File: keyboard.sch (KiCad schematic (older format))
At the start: 29 parts, among them CN2 KEYBOARD_HEADER, U13 MOS_6529, U20 74HCT273

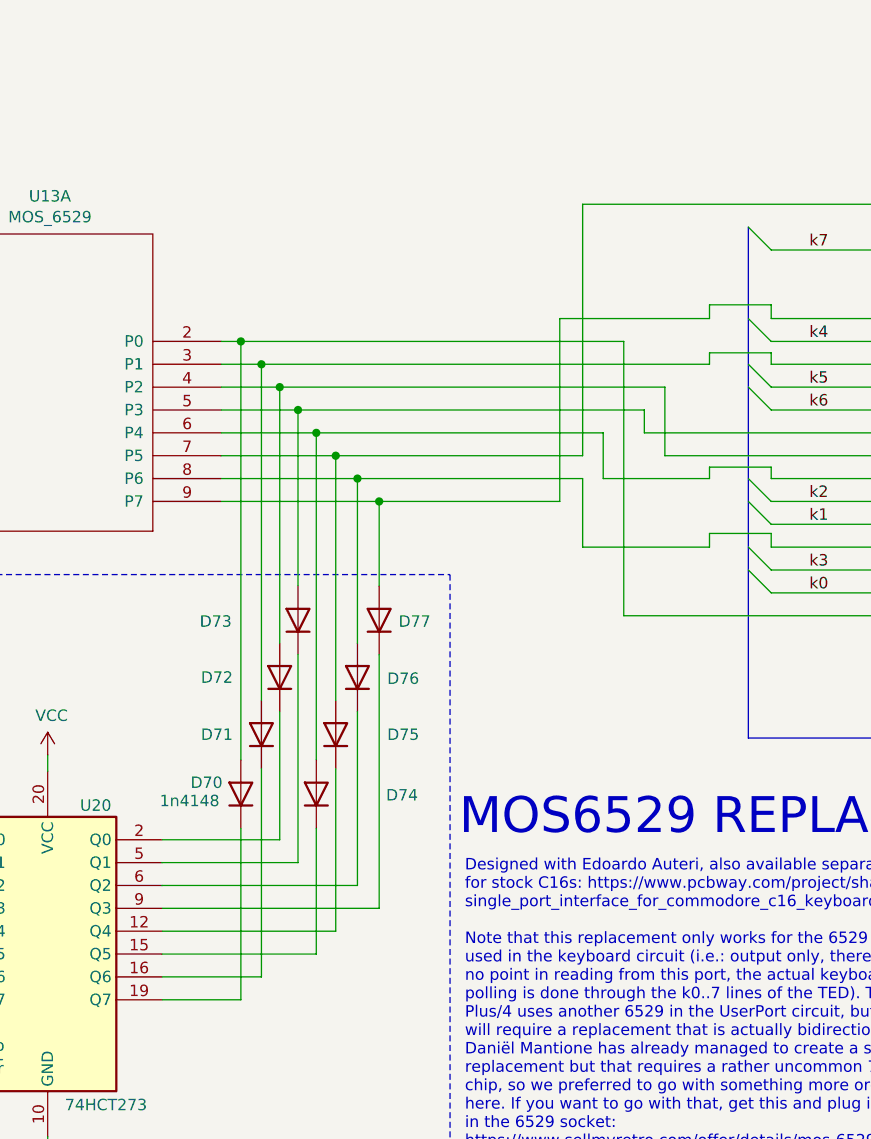
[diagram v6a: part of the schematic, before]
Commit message: Add pull-up network for keyboard buffer Not strictly necessary, boards seems to work fine without, but in principle it should be there
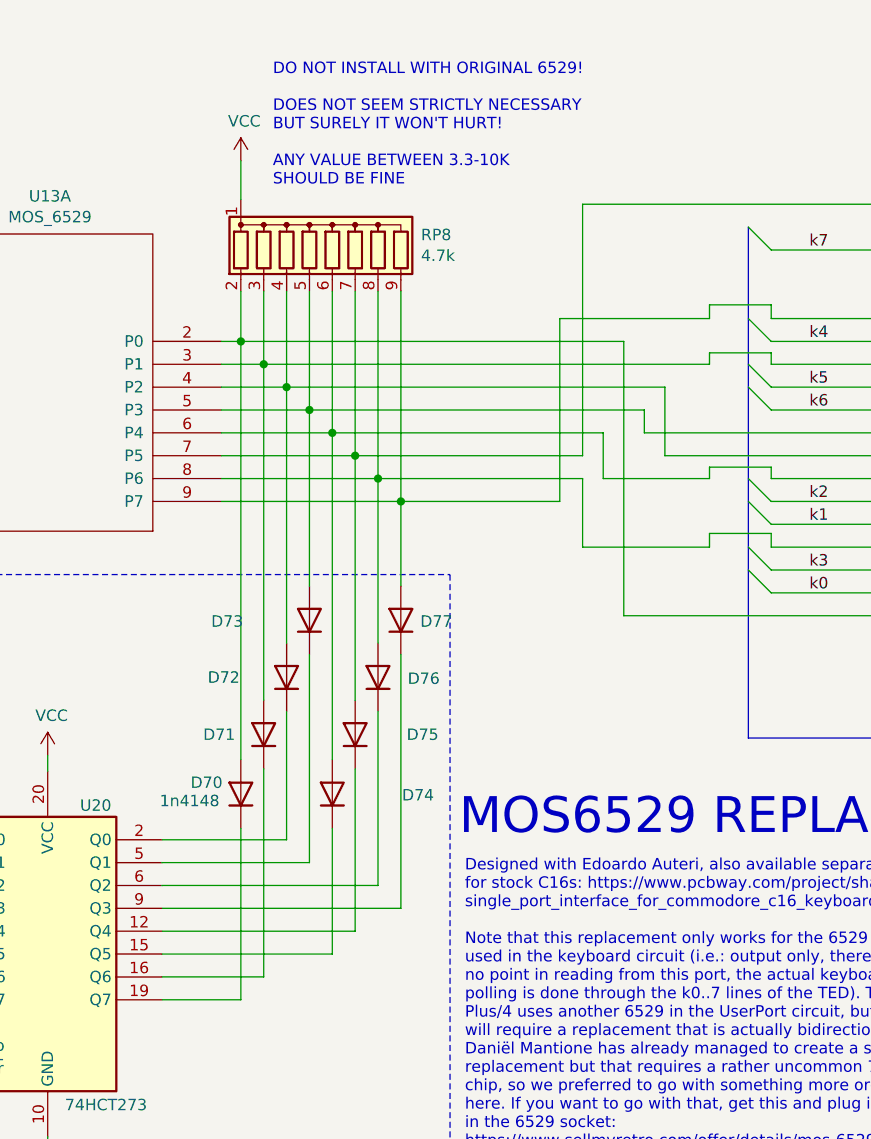
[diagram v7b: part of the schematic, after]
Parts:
- added RP8: 4.7k, Resistor_THT:R_Array_SIP9, symbol Device:R_Network08
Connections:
- net VCC: now also RP8.1 (common)
- net at D70.2 (A), FB41.1, U13.2 (P0): now also RP8.2 (R1)
- net at D71.2 (A), FB42.1, U13.3 (P1): now also RP8.3 (R2)
- net at D72.2 (A), FB43.1, U13.4 (P2): now also RP8.4 (R3)
- net at D73.2 (A), FB44.1, U13.5 (P3): now also RP8.5 (R4)
- net at D74.2 (A), FB45.1, U13.6 (P4): now also RP8.6 (R5)
- net at D75.2 (A), FB46.1, U13.7 (P5): now also RP8.7 (R6)
- net at D76.2 (A), FB47.1, U13.8 (P6): now also RP8.8 (R7)
- net at D77.2 (A), FB48.1, U13.9 (P7): now also RP8.9 (R8)
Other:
- note added: "DO NOT INSTALL WITH ORIGINAL 6529!\n\nDOES NOT SEEM STRICTLY NECESSARY\nBUT SURELY IT WON'T HURT!\n\nANY VALUE BETWEEN 3.3-10K\nSHOULD BE FINE"
- moved on the sheet: D72, D73, D74, D75, D76, D77
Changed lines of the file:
@@
 Sheet 6 14
 Title "LittleSixteen"
-Date "2024-02-05"
+Date "2024-07-21"
 Rev "4git"
 Comp "SukkoPera"
@@
 	7770 2615 8920 2615
 Wire Wire Line
-	5830 2415 6165 2415
-Wire Wire Line
 	7680 2415 7680 2515
 Wire Wire Line
@@
 k[0..7]
 Wire Wire Line
-	5830 2515 6245 2515
-Wire Wire Line
 	7500 2515 7500 2715
-Wire Wire Line
-	5830 2615 6330 2615
 Wire Wire Line
 	7410 1515 7410 2615
@@
 Wire Wire Line
 	8235 1715 8720 1715
-Wire Wire Line
-	5830 2215 6005 2215
-Connection ~ 6005 2215
-Wire Wire Line
-	6005 2215 7965 2215
 Connection ~ 4275 1775
 Wire Wire Line
@@
 Wire Wire Line
 	3605 2815 4330 2815
-Connection ~ 6165 2415
-Wire Wire Line
-	6165 2415 7680 2415
-Connection ~ 6245 2515
-Wire Wire Line
-	6245 2515 7500 2515
-Connection ~ 6520 2815
-Wire Wire Line
-	6520 2815 7310 2815
-Connection ~ 6330 2615
-Wire Wire Line
-	6330 2615 7410 2615
-Connection ~ 6425 2715
-Wire Wire Line
-	6425 2715 7410 2715
-Wire Wire Line
-	5830 2715 6425 2715
-Wire Wire Line
-	5830 2815 6520 2815
 Wire Wire Line
 	5830 2115 5915 2115
 Connection ~ 5915 2115
 Wire Wire Line
-	5830 2315 6085 2315
-Wire Wire Line
-	6085 2315 7770 2315
-Connection ~ 6085 2315
-Wire Wire Line
 	5915 2115 7590 2115
 Wire Wire Line
-	6085 2315 6085 3435
-Wire Wire Line
-	6085 3735 6085 4295
+	6115 2315 6115 3435
+Wire Wire Line
+	6115 3735 6115 4295
 Wire Wire Line
 	5915 2115 5915 3945
 Wire Wire Line
-	6425 2715 6425 3435
+	6515 2715 6515 3435
 Wire Wire Line
 	5070 5680 5070 5595
@@
 L Device:D D72
 U 1 1 61FDC040
-P 6085 3585
-F 0 "D72" V 6085 3930 50  0000 R CNN
-F 1 "1n4148" V 6040 3505 50  0001 R CNN
-F 2 "LittleSixteen:D_DO-35_SOD27_P5.08mm_Vertical_KathodeUp" H 6085 3585 50  0001 C CNN
-F 3 "~" H 6085 3585 50  0001 C CNN
-	1    6085 3585
+P 6115 3585
+F 0 "D72" V 6115 3930 50  0000 R CNN
+F 1 "1n4148" V 6070 3505 50  0001 R CNN
+F 2 "LittleSixteen:D_DO-35_SOD27_P5.08mm_Vertical_KathodeUp" H 6115 3585 50  0001 C CNN
+F 3 "~" H 6115 3585 50  0001 C CNN
+	1    6115 3585
 	0    -1   -1   0
 $EndComp
@@
 L Device:D D71
 U 1 1 61FDBB12
-P 6005 3835
-F 0 "D71" V 6005 4100 50  0000 R CNN
-F 1 "1n4148" V 5960 3755 50  0001 R CNN
-F 2 "LittleSixteen:D_DO-35_SOD27_P5.08mm_Vertical_KathodeUp" H 6005 3835 50  0001 C CNN
-F 3 "~" H 6005 3835 50  0001 C CNN
-	1    6005 3835
+P 6015 3835
+F 0 "D71" V 6015 4100 50  0000 R CNN
+F 1 "1n4148" V 5970 3755 50  0001 R CNN
+F 2 "LittleSixteen:D_DO-35_SOD27_P5.08mm_Vertical_KathodeUp" H 6015 3835 50  0001 C CNN
+F 3 "~" H 6015 3835 50  0001 C CNN
+	1    6015 3835
 	0    -1   -1   0
 $EndComp
@@
 	4275 1775 4275 5195
 Wire Wire Line
-	6005 2215 6005 3685
-Wire Wire Line
-	6330 2615 6330 3685
-Wire Wire Line
-	6245 2515 6245 3945
+	6015 2215 6015 3685
+Wire Wire Line
+	6415 2615 6415 3685
+Wire Wire Line
+	6315 2515 6315 3945
 $Comp
 L Device:D D73
 U 1 1 630E8A8B
-P 6165 3335
-F 0 "D73" V 6160 3765 50  0000 R CNN
-F 1 "1n4148" V 6120 3255 50  0001 R CNN
-F 2 "LittleSixteen:D_DO-35_SOD27_P5.08mm_Vertical_KathodeUp" H 6165 3335 50  0001 C CNN
-F 3 "~" H 6165 3335 50  0001 C CNN
-	1    6165 3335
+P 6215 3335
+F 0 "D73" V 6210 3765 50  0000 R CNN
+F 1 "1n4148" V 6170 3255 50  0001 R CNN
+F 2 "LittleSixteen:D_DO-35_SOD27_P5.08mm_Vertical_KathodeUp" H 6215 3335 50  0001 C CNN
+F 3 "~" H 6215 3335 50  0001 C CNN
+	1    6215 3335
 	0    -1   -1   0
 $EndComp
 Wire Wire Line
-	6165 3185 6165 2415
+	6215 3185 6215 2415
 $Comp
 L Device:D D74
 U 1 1 630E91AD
-P 6245 4095
-F 0 "D74" V 6240 3790 50  0000 R CNN
-F 1 "1n4148" V 6200 4015 50  0001 R CNN
-F 2 "LittleSixteen:D_DO-35_SOD27_P5.08mm_Vertical_KathodeUp" H 6245 4095 50  0001 C CNN
-F 3 "~" H 6245 4095 50  0001 C CNN
-	1    6245 4095
+P 6315 4095
+F 0 "D74" V 6310 3790 50  0000 R CNN
+F 1 "1n4148" V 6270 4015 50  0001 R CNN
+F 2 "LittleSixteen:D_DO-35_SOD27_P5.08mm_Vertical_KathodeUp" H 6315 4095 50  0001 C CNN
+F 3 "~" H 6315 4095 50  0001 C CNN
+	1    6315 4095
 	0    -1   -1   0
 $EndComp
@@
 L Device:D D75
 U 1 1 630E9A0F
-P 6330 3835
-F 0 "D75" V 6330 3610 50  0000 R CNN
-F 1 "1n4148" V 6285 3755 50  0001 R CNN
-F 2 "LittleSixteen:D_DO-35_SOD27_P5.08mm_Vertical_KathodeUp" H 6330 3835 50  0001 C CNN
-F 3 "~" H 6330 3835 50  0001 C CNN
-	1    6330 3835
+P 6415 3835
+F 0 "D75" V 6415 3610 50  0000 R CNN
+F 1 "1n4148" V 6370 3755 50  0001 R CNN
+F 2 "LittleSixteen:D_DO-35_SOD27_P5.08mm_Vertical_KathodeUp" H 6415 3835 50  0001 C CNN
+F 3 "~" H 6415 3835 50  0001 C CNN
+	1    6415 3835
 	0    -1   -1   0
 $EndComp
 Wire Wire Line
-	6330 3985 6330 4695
+	6415 3985 6415 4695
 $Comp
 L Device:D D76
 U 1 1 630EA21C
-P 6425 3585
-F 0 "D76" V 6420 3455 50  0000 R CNN
-F 1 "1n4148" V 6380 3505 50  0001 R CNN
-F 2 "LittleSixteen:D_DO-35_SOD27_P5.08mm_Vertical_KathodeUp" H 6425 3585 50  0001 C CNN
-F 3 "~" H 6425 3585 50  0001 C CNN
-	1    6425 3585
+P 6515 3585
+F 0 "D76" V 6510 3455 50  0000 R CNN
+F 1 "1n4148" V 6470 3505 50  0001 R CNN
+F 2 "LittleSixteen:D_DO-35_SOD27_P5.08mm_Vertical_KathodeUp" H 6515 3585 50  0001 C CNN
+F 3 "~" H 6515 3585 50  0001 C CNN
+	1    6515 3585
 	0    -1   -1   0
 $EndComp
 Wire Wire Line
-	6425 3735 6425 4495
+	6515 3735 6515 4495
 $Comp
 L Device:D D77
 U 1 1 630EAA33
-P 6520 3335
-F 0 "D77" V 6515 3250 50  0000 R CNN
-F 1 "1n4148" V 6475 3255 50  0001 R CNN
-F 2 "LittleSixteen:D_DO-35_SOD27_P5.08mm_Vertical_KathodeUp" H 6520 3335 50  0001 C CNN
-F 3 "~" H 6520 3335 50  0001 C CNN
-	1    6520 3335
+P 6615 3335
+F 0 "D77" V 6610 3250 50  0000 R CNN
+F 1 "1n4148" V 6570 3255 50  0001 R CNN
+F 2 "LittleSixteen:D_DO-35_SOD27_P5.08mm_Vertical_KathodeUp" H 6615 3335 50  0001 C CNN
+F 3 "~" H 6615 3335 50  0001 C CNN
+	1    6615 3335
 	0    -1   -1   0
 $EndComp
 Wire Wire Line
-	6520 3185 6520 2815
+	6615 3185 6615 2815
 $Comp
 L 74xx:74HCT273 U20
@@
 	5915 4245 5915 4995
 Wire Wire Line
-	6005 4895 5570 4895
-Wire Wire Line
-	6005 3985 6005 4895
-Wire Wire Line
-	5570 4295 6085 4295
-Wire Wire Line
-	5570 4395 6165 4395
-Wire Wire Line
-	6165 4395 6165 3485
-Wire Wire Line
-	5570 4795 6245 4795
-Wire Wire Line
-	6245 4245 6245 4795
-Wire Wire Line
-	5570 4695 6330 4695
-Wire Wire Line
-	5570 4495 6425 4495
-Wire Wire Line
-	5570 4595 6520 4595
-Wire Wire Line
-	6520 4595 6520 3485
+	6015 3985 6015 4895
+Wire Wire Line
+	6215 4395 6215 3485
+Wire Wire Line
+	6315 4245 6315 4795
+Wire Wire Line
+	6615 4595 6615 3485
 $Comp
 L Device:Jumper_NO_Small JP1
@@
 Wire Wire Line
 	9185 925  9185 1020
+Text Notes 6055 1440 0    50   ~ 0
+DO NOT INSTALL WITH ORIGINAL 6529!\n\nDOES NOT SEEM STRICTLY NECESSARY\nBUT SURELY IT WON'T HURT!\n\nANY VALUE BETWEEN 3.3-10K\nSHOULD BE FINE
+$Comp
+L power:VCC #PWR?
+U 1 1 66A1641E
+P 5915 1325
+AR Path="/64A6E6F3/66A1641E" Ref="#PWR?"  Part="1"
+AR Path="/5DECEF6F/66A1641E" Ref="#PWR0174"  Part="1"
+F 0 "#PWR0174" H 5915 1175 50  0001 C CNN
+F 1 "VCC" H 5930 1498 50  0000 C CNN
+F 2 "" H 5915 1325 50  0001 C CNN
+F 3 "" H 5915 1325 50  0001 C CNN
+	1    5915 1325
+	1    0    0    -1
+$EndComp
+Wire Wire Line
+	5915 1325 5915 1495
+$Comp
+L Device:R_Network08 RP?
+U 1 1 66A16426
+P 6315 1695
+AR Path="/64A6E6F3/66A16426" Ref="RP?"  Part="1"
+AR Path="/5DECEF6F/66A16426" Ref="RP8"  Part="1"
+F 0 "RP8" H 6703 1741 50  0000 L CNN
+F 1 "4.7k" H 6703 1650 50  0000 L CNN
+F 2 "Resistor_THT:R_Array_SIP9" V 6790 1695 50  0001 C CNN
+F 3 "http://www.vishay.com/docs/31509/csc.pdf" H 6315 1695 50  0001 C CNN
+F 4 "Bussed" H 6315 1695 50  0001 C CNN "Notes"
+	1    6315 1695
+	1    0    0    -1
+$EndComp
+Wire Wire Line
+	5915 1895 5915 2115
+Wire Wire Line
+	6015 1895 6015 2215
+Wire Wire Line
+	6115 1895 6115 2315
+Connection ~ 6115 2315
+Wire Wire Line
+	6115 2315 7770 2315
+Wire Wire Line
+	6215 1895 6215 2415
+Connection ~ 6215 2415
+Wire Wire Line
+	6215 2415 7680 2415
+Wire Wire Line
+	6315 1895 6315 2515
+Connection ~ 6315 2515
+Wire Wire Line
+	6315 2515 7500 2515
+Wire Wire Line
+	6415 1895 6415 2615
+Connection ~ 6415 2615
+Wire Wire Line
+	6415 2615 7410 2615
+Wire Wire Line
+	6515 1895 6515 2715
+Connection ~ 6515 2715
+Wire Wire Line
+	6515 2715 7410 2715
+Wire Wire Line
+	6615 1895 6615 2815
+Connection ~ 6615 2815
+Wire Wire Line
+	6615 2815 7310 2815
+Wire Wire Line
+	5830 2815 6615 2815
+Wire Wire Line
+	5830 2715 6515 2715
+Wire Wire Line
+	5830 2615 6415 2615
+Wire Wire Line
+	5830 2515 6315 2515
+Wire Wire Line
+	5830 2415 6215 2415
+Wire Wire Line
+	5830 2315 6115 2315
+Wire Wire Line
+	5830 2215 6015 2215
+Wire Wire Line
+	5570 4295 6115 4295
+Wire Wire Line
+	5570 4395 6215 4395
+Wire Wire Line
+	5570 4495 6515 4495
+Wire Wire Line
+	5570 4595 6615 4595
+Wire Wire Line
+	5570 4695 6415 4695
+Wire Wire Line
+	5570 4795 6315 4795
+Wire Wire Line
+	5570 4895 6015 4895
+Connection ~ 6015 2215
+Wire Wire Line
+	6015 2215 7965 2215
 Wire Bus Line
 	3090 2015 3090 2720

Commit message: Fix some P/Ns
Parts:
- FB41, FB42, FB43, FB44, FB45, FB46, FB47, FB48, FB49, FB50, FB51, FB52, FB53, FB54, FB55, FB56: value DSS1NB32A271Q91A -> FERRITE; MouserPN (none) -> 623-2743015112
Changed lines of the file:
@@
 P 8810 1515
 F 0 "FB46" V 8665 1515 50  0000 C CNN
-F 1 "DSS1NB32A271Q91A" V 8664 1515 50  0001 C CNN
+F 1 "FERRITE" V 8664 1515 50  0001 C CNN
 F 2 "LittleSixteen:EMI_Filter" V 8740 1515 50  0001 C CNN
 F 3 "~" H 8810 1515 50  0001 C CNN
+F 4 "623-2743015112" H 8810 1515 50  0001 C CNN "MouserPN"
 	1    8810 1515
 	0    -1   1    0
@@
 P 8820 1715
 F 0 "FB56" V 8675 1715 50  0000 C CNN
-F 1 "DSS1NB32A271Q91A" V 8674 1715 50  0001 C CNN
+F 1 "FERRITE" V 8674 1715 50  0001 C CNN
 F 2 "LittleSixteen:EMI_Filter" V 8750 1715 50  0001 C CNN
 F 3 "~" H 8820 1715 50  0001 C CNN
+F 4 "623-2743015112" H 8820 1715 50  0001 C CNN "MouserPN"
 	1    8820 1715
 	0    -1   1    0
@@
 P 8820 2115
 F 0 "FB53" V 8675 2115 50  0000 C CNN
-F 1 "DSS1NB32A271Q91A" V 8674 2115 50  0001 C CNN
+F 1 "FERRITE" V 8674 2115 50  0001 C CNN
 F 2 "LittleSixteen:EMI_Filter" V 8750 2115 50  0001 C CNN
 F 3 "~" H 8820 2115 50  0001 C CNN
+F 4 "623-2743015112" H 8820 2115 50  0001 C CNN "MouserPN"
 	1    8820 2115
 	0    -1   1    0
@@
 P 8830 2315
 F 0 "FB54" V 8685 2315 50  0000 C CNN
-F 1 "DSS1NB32A271Q91A" V 8684 2315 50  0001 C CNN
+F 1 "FERRITE" V 8684 2315 50  0001 C CNN
 F 2 "LittleSixteen:EMI_Filter" V 8760 2315 50  0001 C CNN
 F 3 "~" H 8830 2315 50  0001 C CNN
+F 4 "623-2743015112" H 8830 2315 50  0001 C CNN "MouserPN"
 	1    8830 2315
 	0    -1   1    0
@@
 P 8805 2515
 F 0 "FB44" V 8660 2515 50  0000 C CNN
-F 1 "DSS1NB32A271Q91A" V 8659 2515 50  0001 C CNN
+F 1 "FERRITE" V 8659 2515 50  0001 C CNN
 F 2 "LittleSixteen:EMI_Filter" V 8735 2515 50  0001 C CNN
 F 3 "~" H 8805 2515 50  0001 C CNN
+F 4 "623-2743015112" H 8805 2515 50  0001 C CNN "MouserPN"
 	1    8805 2515
 	0    -1   1    0
@@
 P 8805 2715
 F 0 "FB45" V 8660 2715 50  0000 C CNN
-F 1 "DSS1NB32A271Q91A" V 8659 2715 50  0001 C CNN
+F 1 "FERRITE" V 8659 2715 50  0001 C CNN
 F 2 "LittleSixteen:EMI_Filter" V 8735 2715 50  0001 C CNN
 F 3 "~" H 8805 2715 50  0001 C CNN
+F 4 "623-2743015112" H 8805 2715 50  0001 C CNN "MouserPN"
 	1    8805 2715
 	0    -1   1    0
@@
 P 8815 2915
 F 0 "FB50" V 8670 2915 50  0000 C CNN
-F 1 "DSS1NB32A271Q91A" V 8669 2915 50  0001 C CNN
+F 1 "FERRITE" V 8669 2915 50  0001 C CNN
 F 2 "LittleSixteen:EMI_Filter" V 8745 2915 50  0001 C CNN
 F 3 "~" H 8815 2915 50  0001 C CNN
+F 4 "623-2743015112" H 8815 2915 50  0001 C CNN "MouserPN"
 	1    8815 2915
 	0    -1   1    0
@@
 P 8815 3115
 F 0 "FB52" V 8670 3115 50  0000 C CNN
-F 1 "DSS1NB32A271Q91A" V 8669 3115 50  0001 C CNN
+F 1 "FERRITE" V 8669 3115 50  0001 C CNN
 F 2 "LittleSixteen:EMI_Filter" V 8745 3115 50  0001 C CNN
 F 3 "~" H 8815 3115 50  0001 C CNN
+F 4 "623-2743015112" H 8815 3115 50  0001 C CNN "MouserPN"
 	1    8815 3115
 	0    -1   1    0
@@
 P 8810 3315
 F 0 "FB41" V 8955 3315 50  0000 C CNN
-F 1 "DSS1NB32A271Q91A" V 8664 3315 50  0001 C CNN
+F 1 "FERRITE" V 8664 3315 50  0001 C CNN
 F 2 "LittleSixteen:EMI_Filter" V 8740 3315 50  0001 C CNN
 F 3 "~" H 8810 3315 50  0001 C CNN
+F 4 "623-2743015112" H 8810 3315 50  0001 C CNN "MouserPN"
 	1    8810 3315
 	0    -1   1    0
@@
 P 9030 2015
 F 0 "FB48" V 8885 2015 50  0000 C CNN
-F 1 "DSS1NB32A271Q91A" V 8884 2015 50  0001 C CNN
+F 1 "FERRITE" V 8884 2015 50  0001 C CNN
 F 2 "LittleSixteen:EMI_Filter" V 8960 2015 50  0001 C CNN
 F 3 "~" H 9030 2015 50  0001 C CNN
+F 4 "623-2743015112" H 9030 2015 50  0001 C CNN "MouserPN"
 	1    9030 2015
 	0    -1   1    0
@@
 P 9050 2215
 F 0 "FB42" V 8905 2215 50  0000 C CNN
-F 1 "DSS1NB32A271Q91A" V 8904 2215 50  0001 C CNN
+F 1 "FERRITE" V 8904 2215 50  0001 C CNN
 F 2 "LittleSixteen:EMI_Filter" V 8980 2215 50  0001 C CNN
 F 3 "~" H 9050 2215 50  0001 C CNN
+F 4 "623-2743015112" H 9050 2215 50  0001 C CNN "MouserPN"
 	1    9050 2215
 	0    -1   1    0
@@
 P 9040 2415
 F 0 "FB55" V 8895 2415 50  0000 C CNN
-F 1 "DSS1NB32A271Q91A" V 8894 2415 50  0001 C CNN
+F 1 "FERRITE" V 8894 2415 50  0001 C CNN
 F 2 "LittleSixteen:EMI_Filter" V 8970 2415 50  0001 C CNN
 F 3 "~" H 9040 2415 50  0001 C CNN
+F 4 "623-2743015112" H 9040 2415 50  0001 C CNN "MouserPN"
 	1    9040 2415
 	0    -1   1    0
@@
 P 9020 2615
 F 0 "FB43" V 8875 2615 50  0000 C CNN
-F 1 "DSS1NB32A271Q91A" V 8874 2615 50  0001 C CNN
+F 1 "FERRITE" V 8874 2615 50  0001 C CNN
 F 2 "LittleSixteen:EMI_Filter" V 8950 2615 50  0001 C CNN
 F 3 "~" H 9020 2615 50  0001 C CNN
+F 4 "623-2743015112" H 9020 2615 50  0001 C CNN "MouserPN"
 	1    9020 2615
 	0    -1   1    0
@@
 P 9045 2815
 F 0 "FB51" V 8900 2815 50  0000 C CNN
-F 1 "DSS1NB32A271Q91A" V 8899 2815 50  0001 C CNN
+F 1 "FERRITE" V 8899 2815 50  0001 C CNN
 F 2 "LittleSixteen:EMI_Filter" V 8975 2815 50  0001 C CNN
 F 3 "~" H 9045 2815 50  0001 C CNN
+F 4 "623-2743015112" H 9045 2815 50  0001 C CNN "MouserPN"
 	1    9045 2815
 	0    -1   1    0
@@
 P 9045 3015
 F 0 "FB47" V 8900 3015 50  0000 C CNN
-F 1 "DSS1NB32A271Q91A" V 8899 3015 50  0001 C CNN
+F 1 "FERRITE" V 8899 3015 50  0001 C CNN
 F 2 "LittleSixteen:EMI_Filter" V 8975 3015 50  0001 C CNN
 F 3 "~" H 9045 3015 50  0001 C CNN
+F 4 "623-2743015112" H 9045 3015 50  0001 C CNN "MouserPN"
 	1    9045 3015
 	0    -1   1    0
@@
 P 9030 3215
 F 0 "FB49" V 9150 3215 50  0000 C CNN
-F 1 "DSS1NB32A271Q91A" V 8884 3215 50  0001 C CNN
+F 1 "FERRITE" V 8884 3215 50  0001 C CNN
 F 2 "LittleSixteen:EMI_Filter" V 8960 3215 50  0001 C CNN
 F 3 "~" H 9030 3215 50  0001 C CNN
+F 4 "623-2743015112" H 9030 3215 50  0001 C CNN "MouserPN"
 	1    9030 3215
 	0    -1   1    0
